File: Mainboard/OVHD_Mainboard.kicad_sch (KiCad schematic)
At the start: 0 parts

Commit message: Add the ATmega2560 sheet to the v2 mainboard
The support circuit is the one on the v1 board: four 100 nF and a 10 uF on
the MCU rail, 100 nF on AREF, 10k and 22 pF on RESET, and a 16 MHz 7x5 mm
hand-soldering crystal with two 22 pF.

The pin map comes from the .mfmc, whose 49 buttons were checked against the
as-built copper. Every button keeps its ATmega pin, named as in the .mfmc.
Also on it: the two TLC5927 chains on D22-D27 as in the ShiftRegister
entries, I2C on D20/D21, the UART to the CH340G, the ISP lines, and the
three new outputs, D44 BL_PWM, D45 ANN_PWM and D46 TLC_PWR_EN. The other 21
pins carry no-connect flags. Checked in the exported netlist: all 100 pins
of U301 on the intended nets.

ERC: no errors. The 61 warnings are labels waiting for the connector,
I2C and annunciator sheets.

Co-Authored-By: Claude Opus 5.5 <noreply@anthropic.com>
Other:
- added sheet MCU (mcu.kicad_sch)
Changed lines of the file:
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@@
 	)
 	(sheet
-		(at 30.48 76.2)
+		(at 111.76 40.64)
 		(size 60.96 20.32)
 		(exclude_from_sim no)
@@
 			(color 0 0 0 0)
 		)
-		(property "Sheetname" "USB and supply"
-			(at 30.48 75.5 0)
+		(property "Sheetname" "MCU"
+			(at 111.76 39.94 0)
 			(show_name no)
 			(do_not_autoplace no)
@@
 			)
 		)
-		(property "Sheetfile" "usb_supply.kicad_sch"
-			(at 30.48 97.1 0)
+		(property "Sheetfile" "mcu.kicad_sch"
+			(at 111.76 61.54 0)
 			(show_name no)
 			(do_not_autoplace no)
@@
 		(instances
 			(project "OVHD_Mainboard"
-				(path "/73e7d2ef-26c8-45b7-a17d-3b799e8cb4ab"
-					(page "3")
+				(path "/6b8dd6e4-c4ee-46cc-97f6-84bfaa34cfbf"
+					(page "4")
 				)
 			)
@@
 		(instances
 			(project "OVHD_Mainboard"
-				(path "/73e7d2ef-26c8-45b7-a17d-3b799e8cb4ab"
+				(path "/6b8dd6e4-c4ee-46cc-97f6-84bfaa34cfbf"
 					(page "2")
 				)
 			)
+		)
+	)
+	(sheet
+		(at 30.48 76.2)
+		(size 60.96 20.32)
+		(exclude_from_sim no)
+		(in_bom yes)
+		(on_board yes)
+		(dnp no)
+		(fields_autoplaced yes)
+		(stroke
+			(width 0.1524)
+			(type solid)
+		)
+		(fill
+			(color 0 0 0 0)
+		)
+		(property "Sheetname" "USB and supply"
+			(at 30.48 75.5 0)
+			(show_name no)
+			(do_not_autoplace no)
+			(effects
+				(font
+					(size 1.27 1.27)
+				)
+				(justify left bottom)
+			)
+		)
+		(property "Sheetfile" "usb_supply.kicad_sch"
+			(at 30.48 97.1 0)
+			(show_name no)
+			(do_not_autoplace no)
+			(effects
+				(font
+					(size 1.27 1.27)
+				)
+				(justify left top)
+			)
+		)
+		(instances
+			(project "OVHD_Mainboard"
+				(path "/6b8dd6e4-c4ee-46cc-97f6-84bfaa34cfbf"
+					(page "3")
+				)
+			)

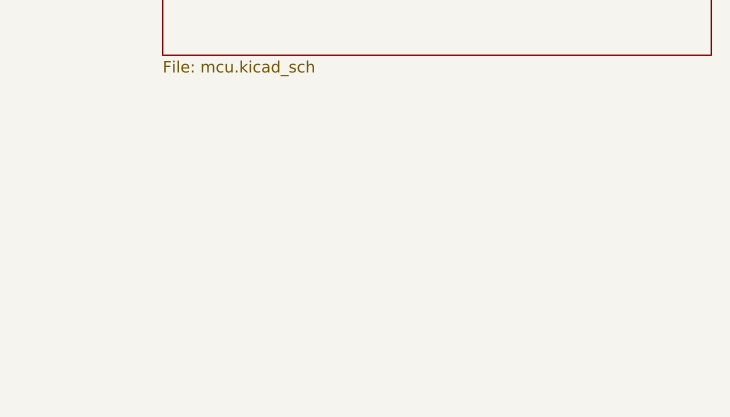
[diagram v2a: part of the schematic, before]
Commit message: Add the I2C sheet to the v2 mainboard
The PCA9548A circuit as on v1, now with KiCad's own PCA9548APW symbol and
footprint (TSSOP-24, the same pinout) instead of the SFLibrary one, which
lives only on one PC. Channels 0, 1 and 2 carry BATT 1, BATT 2 and ADIRS,
as SF_OVHD.h expects, and channels 3-7 carry no-connect flags. The
three-way DIP switch keeps its 10k pull-downs: all off is 0x70, and the
panel runs at 0x71.

The one deliberate change: R402/R403, the pull-ups on the ATmega side, go
to +5V instead of +3V3. An ATmega at 5 V needs 3.5 V to read a high, and
v1 was out of spec there. The PCA9548A, powered at 3.3 V, translates to
the OLED side, which keeps its 4.7k pull-ups to +3V3.

ERC: no errors. SDA and SCL now join the MCU sheet.

Co-Authored-By: Claude Opus 5.5 <noreply@anthropic.com>
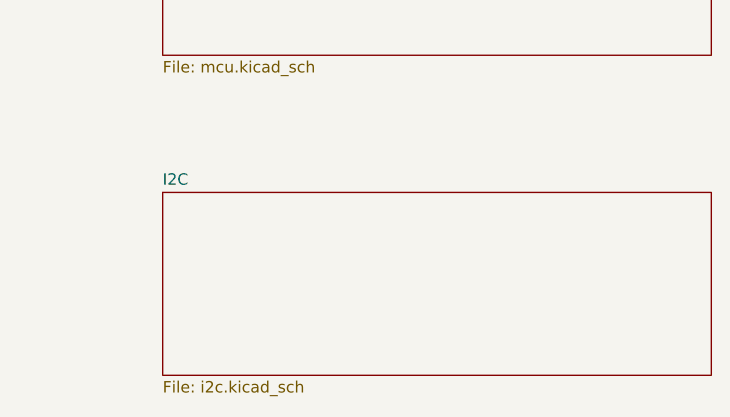
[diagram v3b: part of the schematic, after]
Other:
- added sheet I2C (i2c.kicad_sch)
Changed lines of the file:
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@@
+	)
+	(sheet
+		(at 111.76 76.2)
+		(size 60.96 20.32)
+		(exclude_from_sim no)
+		(in_bom yes)
+		(on_board yes)
+		(dnp no)
+		(fields_autoplaced yes)
+		(stroke
+			(width 0.1524)
+			(type solid)
+		)
+		(fill
+			(color 0 0 0 0)
+		)
+		(property "Sheetname" "I2C"
+			(at 111.76 75.5 0)
+			(show_name no)
+			(do_not_autoplace no)
+			(effects
+				(font
+					(size 1.27 1.27)
+				)
+				(justify left bottom)
+			)
+		)
+		(property "Sheetfile" "i2c.kicad_sch"
+			(at 111.76 97.1 0)
+			(show_name no)
+			(do_not_autoplace no)
+			(effects
+				(font
+					(size 1.27 1.27)
+				)
+				(justify left top)
+			)
+		)
+		(instances
+			(project "OVHD_Mainboard"
+				(path "/41250dd4-2159-4b7d-88fc-4463c1b04a92"
+					(page "5")
+				)
+			)
+		)
+	)
+	(sheet
+		(at 30.48 76.2)
+		(size 60.96 20.32)
+		(exclude_from_sim no)
+		(in_bom yes)
+		(on_board yes)
+		(dnp no)
+		(fields_autoplaced yes)
+		(stroke
+			(width 0.1524)
+			(type solid)
+		)
+		(fill
+			(color 0 0 0 0)
+		)
+		(property "Sheetname" "USB and supply"
+			(at 30.48 75.5 0)
+			(show_name no)
+			(do_not_autoplace no)
+			(effects
+				(font
+					(size 1.27 1.27)
+				)
+				(justify left bottom)
+			)
+		)
+		(property "Sheetfile" "usb_supply.kicad_sch"
+			(at 30.48 97.1 0)
+			(show_name no)
+			(do_not_autoplace no)
+			(effects
+				(font
+					(size 1.27 1.27)
+				)
+				(justify left top)
+			)
+		)
+		(instances
+			(project "OVHD_Mainboard"
+				(path "/41250dd4-2159-4b7d-88fc-4463c1b04a92"
+					(page "3")
+				)
+			)
+		)
 	)
 	(sheet
@@
 		(instances
 			(project "OVHD_Mainboard"
-				(path "/6b8dd6e4-c4ee-46cc-97f6-84bfaa34cfbf"
+				(path "/41250dd4-2159-4b7d-88fc-4463c1b04a92"
 					(page "4")
 				)
@@
 		(instances
 			(project "OVHD_Mainboard"
-				(path "/6b8dd6e4-c4ee-46cc-97f6-84bfaa34cfbf"
+				(path "/41250dd4-2159-4b7d-88fc-4463c1b04a92"
 					(page "2")
 				)
 			)
-		)
-	)
-	(sheet
-		(at 30.48 76.2)
-		(size 60.96 20.32)
-		(exclude_from_sim no)
-		(in_bom yes)
-		(on_board yes)
-		(dnp no)
-		(fields_autoplaced yes)
-		(stroke
-			(width 0.1524)
-			(type solid)
-		)
-		(fill
-			(color 0 0 0 0)
-		)
-		(property "Sheetname" "USB and supply"
-			(at 30.48 75.5 0)
-			(show_name no)
-			(do_not_autoplace no)
-			(effects
-				(font
-					(size 1.27 1.27)
-				)
-				(justify left bottom)
-			)
-		)
-		(property "Sheetfile" "usb_supply.kicad_sch"
-			(at 30.48 97.1 0)
-			(show_name no)
-			(do_not_autoplace no)
-			(effects
-				(font
-					(size 1.27 1.27)
-				)
-				(justify left top)
-			)
-		)
-		(instances
-			(project "OVHD_Mainboard"
-				(path "/6b8dd6e4-c4ee-46cc-97f6-84bfaa34cfbf"
-					(page "3")
-				)
-			)

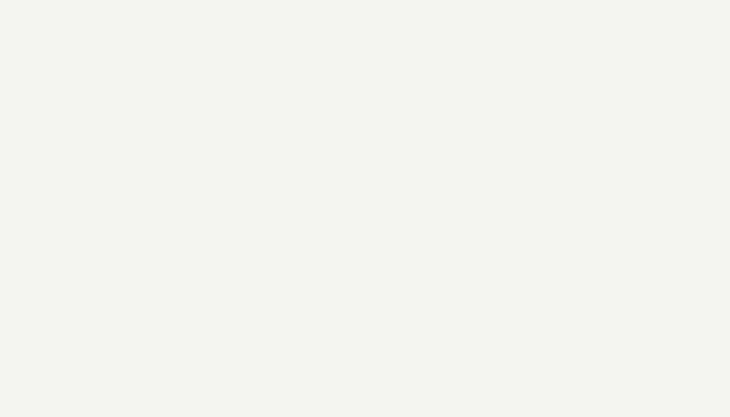
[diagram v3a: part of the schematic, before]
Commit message: Add the annunciator sheet: four TLC5927 and their two supply switches
The two chains of v1 with TI TLC5927IDWR: ANN_LOWER (D22/23/24) into U501
white then U502 blue, ANN_UPPER (D25/26/27) into U503 amber then U504
green/amber. Each of the 44 outputs is named after the LED its copper
reaches on the as-built v1. The 20 unused ones carry no-connect flags.

Per chip: R-EXT 1k (19 mA per LED, the value fitted on the current board),
100 nF on VDD, and a 100 nF on R-EXT placed but marked DNP, since the
TLC5927 datasheet does not ask for it. OE is tied hard to GND, because it
is also the mode pin. Each CLK, LE and first-SDI line has 1k in series at
the chip, so an unpowered chip is not fed through its inputs.

Two identical AO3401A high-side switches, each driven by a BS170 with 100R
into the gate and 100k to ground, a 10k pull-up holding the P-FET off:
- +5V_LED, the LED anodes, from 5V_EXT, PWM'd by D45 (ANN_PWM) for dimming;
- +5V_TLC, the chips' VDD, from +5V, turned on by D46 (TLC_PWR_EN) once
  the firmware is running.
With D45 or D46 low or undriven, both stay off.

The Digi-Key symbol typed OE as an output, the sinks as plain outputs and
R-EXT as an input. The local library now has OE as an input, OUT0-15 as
open collector and R-EXT as passive, patched by the build script.

ERC: no errors. The netlist has the chains, both rails and all 44 LED nets
on the intended pins.

Co-Authored-By: Claude Opus 5.5 <noreply@anthropic.com>
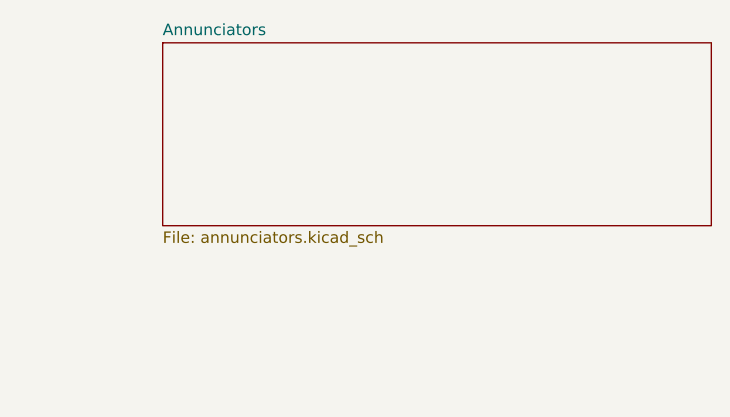
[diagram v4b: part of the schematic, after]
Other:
- added sheet Annunciators (annunciators.kicad_sch)
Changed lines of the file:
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@@
+	)
+	(sheet
+		(at 193.04 40.64)
+		(size 60.96 20.32)
+		(exclude_from_sim no)
+		(in_bom yes)
+		(on_board yes)
+		(dnp no)
+		(fields_autoplaced yes)
+		(stroke
+			(width 0.1524)
+			(type solid)
+		)
+		(fill
+			(color 0 0 0 0)
+		)
+		(property "Sheetname" "Annunciators"
+			(at 193.04 39.94 0)
+			(show_name no)
+			(do_not_autoplace no)
+			(effects
+				(font
+					(size 1.27 1.27)
+				)
+				(justify left bottom)
+			)
+		)
+		(property "Sheetfile" "annunciators.kicad_sch"
+			(at 193.04 61.54 0)
+			(show_name no)
+			(do_not_autoplace no)
+			(effects
+				(font
+					(size 1.27 1.27)
+				)
+				(justify left top)
+			)
+		)
+		(instances
+			(project "OVHD_Mainboard"
+				(path "/52924ed9-850d-44ae-9796-844fad281947"
+					(page "6")
+				)
+			)
+		)
+	)
+	(sheet
+		(at 30.48 76.2)
+		(size 60.96 20.32)
+		(exclude_from_sim no)
+		(in_bom yes)
+		(on_board yes)
+		(dnp no)
+		(fields_autoplaced yes)
+		(stroke
+			(width 0.1524)
+			(type solid)
+		)
+		(fill
+			(color 0 0 0 0)
+		)
+		(property "Sheetname" "USB and supply"
+			(at 30.48 75.5 0)
+			(show_name no)
+			(do_not_autoplace no)
+			(effects
+				(font
+					(size 1.27 1.27)
+				)
+				(justify left bottom)
+			)
+		)
+		(property "Sheetfile" "usb_supply.kicad_sch"
+			(at 30.48 97.1 0)
+			(show_name no)
+			(do_not_autoplace no)
+			(effects
+				(font
+					(size 1.27 1.27)
+				)
+				(justify left top)
+			)
+		)
+		(instances
+			(project "OVHD_Mainboard"
+				(path "/52924ed9-850d-44ae-9796-844fad281947"
+					(page "3")
+				)
+			)
+		)
+	)
+	(sheet
+		(at 111.76 40.64)
+		(size 60.96 20.32)
+		(exclude_from_sim no)
+		(in_bom yes)
+		(on_board yes)
+		(dnp no)
+		(fields_autoplaced yes)
+		(stroke
+			(width 0.1524)
+			(type solid)
+		)
+		(fill
+			(color 0 0 0 0)
+		)
+		(property "Sheetname" "MCU"
+			(at 111.76 39.94 0)
+			(show_name no)
+			(do_not_autoplace no)
+			(effects
+				(font
+					(size 1.27 1.27)
+				)
+				(justify left bottom)
+			)
+		)
+		(property "Sheetfile" "mcu.kicad_sch"
+			(at 111.76 61.54 0)
+			(show_name no)
+			(do_not_autoplace no)
+			(effects
+				(font
+					(size 1.27 1.27)
+				)
+				(justify left top)
+			)
+		)
+		(instances
+			(project "OVHD_Mainboard"
+				(path "/52924ed9-850d-44ae-9796-844fad281947"
+					(page "4")
+				)
+			)
+		)
+	)
+	(sheet
+		(at 30.48 40.64)
+		(size 60.96 20.32)
+		(exclude_from_sim no)
+		(in_bom yes)
+		(on_board yes)
+		(dnp no)
+		(fields_autoplaced yes)
+		(stroke
+			(width 0.1524)
+			(type solid)
+		)
+		(fill
+			(color 0 0 0 0)
+		)
+		(property "Sheetname" "Power"
+			(at 30.48 39.94 0)
+			(show_name no)
+			(do_not_autoplace no)
+			(effects
+				(font
+					(size 1.27 1.27)
+				)
+				(justify left bottom)
+			)
+		)
+		(property "Sheetfile" "power.kicad_sch"
+			(at 30.48 61.54 0)
+			(show_name no)
+			(do_not_autoplace no)
+			(effects
+				(font
+					(size 1.27 1.27)
+				)
+				(justify left top)
+			)
+		)
+		(instances
+			(project "OVHD_Mainboard"
+				(path "/52924ed9-850d-44ae-9796-844fad281947"
+					(page "2")
+				)
+			)
+		)
 	)
 	(sheet
@@
 		(instances
 			(project "OVHD_Mainboard"
-				(path "/41250dd4-2159-4b7d-88fc-4463c1b04a92"
+				(path "/52924ed9-850d-44ae-9796-844fad281947"
 					(page "5")
 				)
 			)
-		)
-	)
-	(sheet
-		(at 30.48 76.2)
-		(size 60.96 20.32)
-		(exclude_from_sim no)
-		(in_bom yes)
-		(on_board yes)
-		(dnp no)
-		(fields_autoplaced yes)
-		(stroke
-			(width 0.1524)
-			(type solid)
-		)
-		(fill
-			(color 0 0 0 0)
-		)
-		(property "Sheetname" "USB and supply"
-			(at 30.48 75.5 0)
-			(show_name no)
-			(do_not_autoplace no)
-			(effects
-				(font
-					(size 1.27 1.27)
-				)
-				(justify left bottom)
-			)
-		)
-		(property "Sheetfile" "usb_supply.kicad_sch"
-			(at 30.48 97.1 0)
-			(show_name no)
-			(do_not_autoplace no)
-			(effects
-				(font
-					(size 1.27 1.27)
-				)
-				(justify left top)
-			)
-		)
-		(instances
-			(project "OVHD_Mainboard"
-				(path "/41250dd4-2159-4b7d-88fc-4463c1b04a92"
-					(page "3")
-				)
-			)
-		)
-	)
-	(sheet
-		(at 111.76 40.64)
-		(size 60.96 20.32)
-		(exclude_from_sim no)
-		(in_bom yes)
-		(on_board yes)
-		(dnp no)
-		(fields_autoplaced yes)
-		(stroke
-			(width 0.1524)
-			(type solid)
-		)
-		(fill
-			(color 0 0 0 0)
-		)
-		(property "Sheetname" "MCU"
-			(at 111.76 39.94 0)
-			(show_name no)
-			(do_not_autoplace no)
-			(effects
-				(font
-					(size 1.27 1.27)
-				)
-				(justify left bottom)
-			)
-		)
-		(property "Sheetfile" "mcu.kicad_sch"
-			(at 111.76 61.54 0)
-			(show_name no)
-			(do_not_autoplace no)
-			(effects
-				(font
-					(size 1.27 1.27)
-				)
-				(justify left top)
-			)
-		)
-		(instances
-			(project "OVHD_Mainboard"
-				(path "/41250dd4-2159-4b7d-88fc-4463c1b04a92"
-					(page "4")
-				)
-			)
-		)
-	)
-	(sheet
-		(at 30.48 40.64)
-		(size 60.96 20.32)
-		(exclude_from_sim no)
-		(in_bom yes)
-		(on_board yes)
-		(dnp no)
-		(fields_autoplaced yes)
-		(stroke
-			(width 0.1524)
-			(type solid)
-		)
-		(fill
-			(color 0 0 0 0)
-		)
-		(property "Sheetname" "Power"
-			(at 30.48 39.94 0)
-			(show_name no)
-			(do_not_autoplace no)
-			(effects
-				(font
-					(size 1.27 1.27)
-				)
-				(justify left bottom)
-			)
-		)
-		(property "Sheetfile" "power.kicad_sch"
-			(at 30.48 61.54 0)
-			(show_name no)
-			(do_not_autoplace no)
-			(effects
-				(font
-					(size 1.27 1.27)
-				)
-				(justify left top)
-			)
-		)
-		(instances
-			(project "OVHD_Mainboard"
-				(path "/41250dd4-2159-4b7d-88fc-4463c1b04a92"
-					(page "2")
-				)
-			)

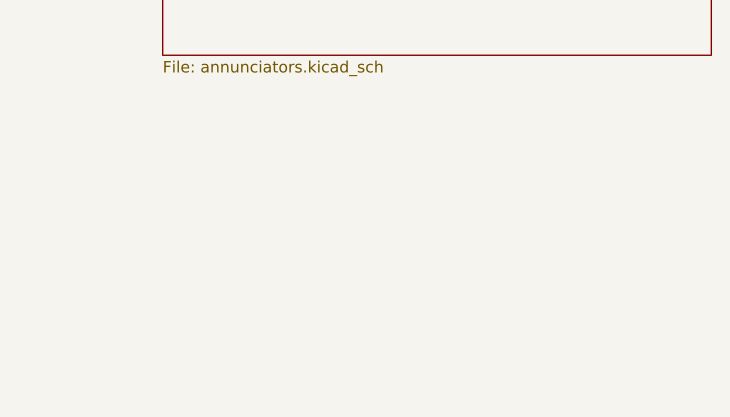
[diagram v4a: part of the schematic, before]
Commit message: Complete the mainboard schematic: backlight switch and the eight connectors
The last sheet carries the backlight dimmer and the section-board
connectors. The dimmer is an IRLIZ44N low-side switch, as on the FCU, gated
from D44 through 100R with a 10k pull-down. Each section board gets a
shrouded IDC header with the pinout in docs/board-split.md, 136 pins over
eight headers, and a 5.08 mm two-pole terminal for its backlight, +9V_BL
and the switched return.

The whole schematic now passes the ERC with no errors and no warnings.
Checked on the exported netlist: each of the 49 .mfmc buttons runs from its
v1 ATmega pin to exactly one ribbon pin; each of the 44 annunciators from
its TLC5927 output to exactly one ribbon pin; every IDC pin matches the
table in the plan.

The plan gains a short status section listing the parts chosen while
drawing, for review.

Co-Authored-By: Claude Opus 5.5 <noreply@anthropic.com>
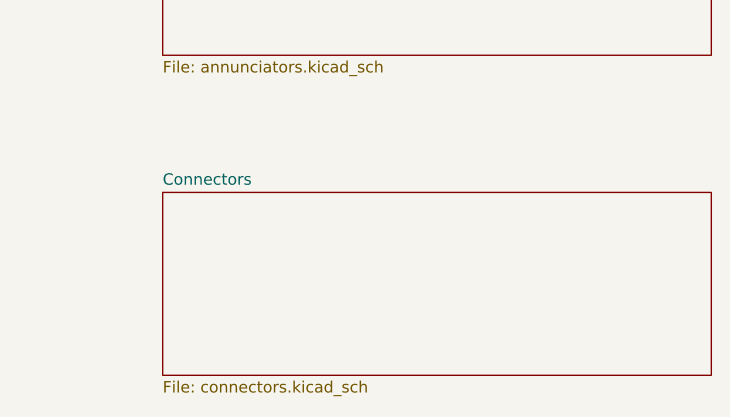
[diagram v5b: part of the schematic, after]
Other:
- added sheet Connectors (connectors.kicad_sch)
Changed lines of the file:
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@@
+	)
+	(sheet
+		(at 111.76 76.2)
+		(size 60.96 20.32)
+		(exclude_from_sim no)
+		(in_bom yes)
+		(on_board yes)
+		(dnp no)
+		(fields_autoplaced yes)
+		(stroke
+			(width 0.1524)
+			(type solid)
+		)
+		(fill
+			(color 0 0 0 0)
+		)
+		(property "Sheetname" "I2C"
+			(at 111.76 75.5 0)
+			(show_name no)
+			(do_not_autoplace no)
+			(effects
+				(font
+					(size 1.27 1.27)
+				)
+				(justify left bottom)
+			)
+		)
+		(property "Sheetfile" "i2c.kicad_sch"
+			(at 111.76 97.1 0)
+			(show_name no)
+			(do_not_autoplace no)
+			(effects
+				(font
+					(size 1.27 1.27)
+				)
+				(justify left top)
+			)
+		)
+		(instances
+			(project "OVHD_Mainboard"
+				(path "/b1fa8af7-a458-4307-9f26-c3f25469de48"
+					(page "5")
+				)
+			)
+		)
+	)
+	(sheet
+		(at 30.48 40.64)
+		(size 60.96 20.32)
+		(exclude_from_sim no)
+		(in_bom yes)
+		(on_board yes)
+		(dnp no)
+		(fields_autoplaced yes)
+		(stroke
+			(width 0.1524)
+			(type solid)
+		)
+		(fill
+			(color 0 0 0 0)
+		)
+		(property "Sheetname" "Power"
+			(at 30.48 39.94 0)
+			(show_name no)
+			(do_not_autoplace no)
+			(effects
+				(font
+					(size 1.27 1.27)
+				)
+				(justify left bottom)
+			)
+		)
+		(property "Sheetfile" "power.kicad_sch"
+			(at 30.48 61.54 0)
+			(show_name no)
+			(do_not_autoplace no)
+			(effects
+				(font
+					(size 1.27 1.27)
+				)
+				(justify left top)
+			)
+		)
+		(instances
+			(project "OVHD_Mainboard"
+				(path "/b1fa8af7-a458-4307-9f26-c3f25469de48"
+					(page "2")
+				)
+			)
+		)
 	)
 	(sheet
@@
 		(instances
 			(project "OVHD_Mainboard"
-				(path "/52924ed9-850d-44ae-9796-844fad281947"
+				(path "/b1fa8af7-a458-4307-9f26-c3f25469de48"
 					(page "6")
+				)
+			)
+		)
+	)
+	(sheet
+		(at 193.04 76.2)
+		(size 60.96 20.32)
+		(exclude_from_sim no)
+		(in_bom yes)
+		(on_board yes)
+		(dnp no)
+		(fields_autoplaced yes)
+		(stroke
+			(width 0.1524)
+			(type solid)
+		)
+		(fill
+			(color 0 0 0 0)
+		)
+		(property "Sheetname" "Connectors"
+			(at 193.04 75.5 0)
+			(show_name no)
+			(do_not_autoplace no)
+			(effects
+				(font
+					(size 1.27 1.27)
+				)
+				(justify left bottom)
+			)
+		)
+		(property "Sheetfile" "connectors.kicad_sch"
+			(at 193.04 97.1 0)
+			(show_name no)
+			(do_not_autoplace no)
+			(effects
+				(font
+					(size 1.27 1.27)
+				)
+				(justify left top)
+			)
+		)
+		(instances
+			(project "OVHD_Mainboard"
+				(path "/b1fa8af7-a458-4307-9f26-c3f25469de48"
+					(page "7")
 				)
 			)
@@
 		(instances
 			(project "OVHD_Mainboard"
-				(path "/52924ed9-850d-44ae-9796-844fad281947"
+				(path "/b1fa8af7-a458-4307-9f26-c3f25469de48"
 					(page "3")
 				)
@@
 		(instances
 			(project "OVHD_Mainboard"
-				(path "/52924ed9-850d-44ae-9796-844fad281947"
+				(path "/b1fa8af7-a458-4307-9f26-c3f25469de48"
 					(page "4")
 				)
 			)
-		)
-	)
-	(sheet
-		(at 30.48 40.64)
-		(size 60.96 20.32)
-		(exclude_from_sim no)
-		(in_bom yes)
-		(on_board yes)
-		(dnp no)
-		(fields_autoplaced yes)
-		(stroke
-			(width 0.1524)
-			(type solid)
-		)
-		(fill
-			(color 0 0 0 0)
-		)
-		(property "Sheetname" "Power"
-			(at 30.48 39.94 0)
-			(show_name no)
-			(do_not_autoplace no)
-			(effects
-				(font
-					(size 1.27 1.27)
-				)
-				(justify left bottom)
-			)
-		)
-		(property "Sheetfile" "power.kicad_sch"
-			(at 30.48 61.54 0)
-			(show_name no)
-			(do_not_autoplace no)
-			(effects
-				(font
-					(size 1.27 1.27)
-				)
-				(justify left top)
-			)
-		)
-		(instances
-			(project "OVHD_Mainboard"
-				(path "/52924ed9-850d-44ae-9796-844fad281947"
-					(page "2")
-				)
-			)
-		)
-	)
-	(sheet
-		(at 111.76 76.2)
-		(size 60.96 20.32)
-		(exclude_from_sim no)
-		(in_bom yes)
-		(on_board yes)
-		(dnp no)
-		(fields_autoplaced yes)
-		(stroke
-			(width 0.1524)
-			(type solid)
-		)
-		(fill
-			(color 0 0 0 0)
-		)
-		(property "Sheetname" "I2C"
-			(at 111.76 75.5 0)
-			(show_name no)
-			(do_not_autoplace no)
-			(effects
-				(font
-					(size 1.27 1.27)
-				)
-				(justify left bottom)
-			)
-		)
-		(property "Sheetfile" "i2c.kicad_sch"
-			(at 111.76 97.1 0)
-			(show_name no)
-			(do_not_autoplace no)
-			(effects
-				(font
-					(size 1.27 1.27)
-				)
-				(justify left top)
-			)
-		)
-		(instances
-			(project "OVHD_Mainboard"
-				(path "/52924ed9-850d-44ae-9796-844fad281947"
-					(page "5")
-				)
-			)
